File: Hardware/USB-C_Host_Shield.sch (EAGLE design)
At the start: 20 parts, among them U1 ARDUINO_UNO_R3_SHIELDBASIC, U4 AP7361C-33FGEUDFN-8

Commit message: Continued work on schematic
Working on importing new component now
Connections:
- net N$1 renamed VIN
- removed net N$9: C8.1, R1.2, U4.OUT
- new net GPX: U1.D8
- new net INT: U1.*D9
- new net MISO: U1.D12
- new net MOSI: U1.*D11
- new net N$15: U1.SDA
- new net N$16: U1.SCL
- new net RESET: U1.D7
- new net SCK: U1.D13
- new net SS: U1.*D10
- net 3.3V: now also C8.1, R1.2, U4.OUT
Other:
- moved on the sheet: U1
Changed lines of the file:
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@@
 <class number="0" name="default" width="0" drill="0">
+</class>
+<class number="1" name="VIN" width="0" drill="0">
 </class>
 </classes>
@@
 <part name="C6" library="SparkFun-Capacitors" deviceset="10UF-POLAR" device="-EIA3216-16V-10%(TANT)" value="10uF"/>
 <part name="GND3" library="SparkFun-PowerSymbols" deviceset="GND" device=""/>
-<part name="GND4" library="SparkFun-PowerSymbols" deviceset="GND" device=""/>
 <part name="C7" library="SparkFun-Capacitors" deviceset="10UF-POLAR" device="-EIA3216-16V-10%(TANT)" value="10uF"/>
 <part name="GND5" library="SparkFun-PowerSymbols" deviceset="GND" device=""/>
@@
 <part name="GND7" library="SparkFun-PowerSymbols" deviceset="GND" device=""/>
 <part name="R1" library="SparkFun-Resistors" deviceset="1KOHM" device="-0603-1/10W-1%" value="1k"/>
+<part name="GND4" library="SparkFun-PowerSymbols" deviceset="GND" device=""/>
+<part name="SUPPLY2" library="SparkFun-PowerSymbols" deviceset="3.3V" device=""/>
 </parts>
 <sheets>
@@
 <instance part="FD3" gate="G$1" x="226.06" y="30.48" smashed="yes"/>
 <instance part="FD4" gate="G$1" x="231.14" y="27.94" smashed="yes"/>
-<instance part="U1" gate="G$1" x="48.26" y="96.52" smashed="yes">
-<attribute name="NAME" x="38.608" y="117.094" size="1.778" layer="95" font="vector"/>
-<attribute name="VALUE" x="39.37" y="70.866" size="1.778" layer="96" font="vector" align="top-left"/>
+<instance part="U1" gate="G$1" x="58.42" y="71.12" smashed="yes">
+<attribute name="NAME" x="48.768" y="91.694" size="1.778" layer="95" font="vector"/>
+<attribute name="VALUE" x="49.53" y="45.466" size="1.778" layer="96" font="vector" align="top-left"/>
 </instance>
 <instance part="J1" gate="J1" x="127" y="111.76" smashed="yes">
@@
 <attribute name="VALUE" x="193.04" y="124.206" size="1.778" layer="96" font="vector" align="top-center"/>
 </instance>
-<instance part="GND2" gate="1" x="30.48" y="66.04" smashed="yes">
-<attribute name="VALUE" x="30.48" y="65.786" size="1.778" layer="96" font="vector" align="top-center"/>
+<instance part="GND2" gate="1" x="40.64" y="40.64" smashed="yes">
+<attribute name="VALUE" x="40.64" y="40.386" size="1.778" layer="96" font="vector" align="top-center"/>
 </instance>
 <instance part="C6" gate="G$1" x="71.12" y="154.94" smashed="yes">
@@
 <attribute name="VALUE" x="66.04" y="139.446" size="1.778" layer="96" font="vector" align="top-center"/>
 </instance>
-<instance part="GND4" gate="1" x="83.82" y="132.08" smashed="yes">
-<attribute name="VALUE" x="83.82" y="131.826" size="1.778" layer="96" font="vector" align="top-center"/>
-</instance>
 <instance part="C7" gate="G$1" x="111.76" y="154.94" smashed="yes">
 <attribute name="NAME" x="112.776" y="155.575" size="1.778" layer="95" font="vector"/>
@@
 <attribute name="NAME" x="161.036" y="152.4" size="1.778" layer="95" font="vector" rot="R90" align="bottom-center"/>
 <attribute name="VALUE" x="164.084" y="152.4" size="1.778" layer="96" font="vector" rot="R90" align="top-center"/>
+</instance>
+<instance part="GND4" gate="1" x="93.98" y="134.62" smashed="yes">
+<attribute name="VALUE" x="93.98" y="134.366" size="1.778" layer="96" font="vector" align="top-center"/>
+</instance>
+<instance part="SUPPLY2" gate="G$1" x="162.56" y="162.56" smashed="yes">
+<attribute name="VALUE" x="162.56" y="165.354" size="1.778" layer="96" font="vector" align="bottom-center"/>
 </instance>
 </instances>
@@
 </busses>
 <nets>
-<net name="N$1" class="0">
+<net name="VIN" class="0">
 <segment>
 <pinref part="S1" gate="G$1" pin="2"/>
@@
 <junction x="33.02" y="157.48"/>
 <wire x1="22.86" y1="157.48" x2="33.02" y2="157.48" width="0.1524" layer="91"/>
+<label x="22.86" y="157.48" size="1.27" layer="95"/>
 </segment>
 </net>
@@
 <junction x="193.04" y="142.24"/>
 </segment>
+<segment>
+<wire x1="142.24" y1="160.02" x2="147.32" y2="160.02" width="0.1524" layer="91"/>
+<pinref part="U4" gate="G$1" pin="OUT"/>
+<pinref part="C8" gate="G$1" pin="1"/>
+<wire x1="147.32" y1="157.48" x2="147.32" y2="160.02" width="0.1524" layer="91"/>
+<wire x1="147.32" y1="160.02" x2="162.56" y2="160.02" width="0.1524" layer="91"/>
+<junction x="147.32" y="160.02"/>
+<wire x1="162.56" y1="160.02" x2="162.56" y2="157.48" width="0.1524" layer="91"/>
+<pinref part="R1" gate="G$1" pin="2"/>
+<wire x1="162.56" y1="160.02" x2="162.56" y2="162.56" width="0.1524" layer="91"/>
+<junction x="162.56" y="160.02"/>
+<pinref part="SUPPLY2" gate="G$1" pin="3.3V"/>
+</segment>
 </net>
 <net name="GND" class="0">
@@
 <pinref part="U1" gate="G$1" pin="GND@2"/>
 <pinref part="GND2" gate="1" pin="GND"/>
-<wire x1="35.56" y1="78.74" x2="30.48" y2="78.74" width="0.1524" layer="91"/>
-<wire x1="30.48" y1="78.74" x2="30.48" y2="76.2" width="0.1524" layer="91"/>
+<wire x1="45.72" y1="53.34" x2="40.64" y2="53.34" width="0.1524" layer="91"/>
+<wire x1="40.64" y1="53.34" x2="40.64" y2="50.8" width="0.1524" layer="91"/>
 <pinref part="U1" gate="G$1" pin="GND@1"/>
-<wire x1="30.48" y1="76.2" x2="30.48" y2="73.66" width="0.1524" layer="91"/>
-<wire x1="30.48" y1="73.66" x2="30.48" y2="68.58" width="0.1524" layer="91"/>
-<wire x1="35.56" y1="76.2" x2="30.48" y2="76.2" width="0.1524" layer="91"/>
-<junction x="30.48" y="76.2"/>
+<wire x1="40.64" y1="50.8" x2="40.64" y2="48.26" width="0.1524" layer="91"/>
+<wire x1="40.64" y1="48.26" x2="40.64" y2="43.18" width="0.1524" layer="91"/>
+<wire x1="45.72" y1="50.8" x2="40.64" y2="50.8" width="0.1524" layer="91"/>
+<junction x="40.64" y="50.8"/>
 <pinref part="U1" gate="G$1" pin="GND@0"/>
-<wire x1="35.56" y1="73.66" x2="30.48" y2="73.66" width="0.1524" layer="91"/>
-<junction x="30.48" y="73.66"/>
+<wire x1="45.72" y1="48.26" x2="40.64" y2="48.26" width="0.1524" layer="91"/>
+<junction x="40.64" y="48.26"/>
 </segment>
 <segment>
@@
 </segment>
 </net>
-<net name="N$4" class="0">
-<segment>
-<pinref part="U2" gate="G$1" pin="ADJ"/>
-<wire x1="83.82" y1="152.4" x2="83.82" y2="147.32" width="0.1524" layer="91"/>
-<wire x1="83.82" y1="147.32" x2="93.98" y2="147.32" width="0.1524" layer="91"/>
-<wire x1="93.98" y1="147.32" x2="93.98" y2="149.86" width="0.1524" layer="91"/>
-<wire x1="83.82" y1="147.32" x2="83.82" y2="144.78" width="0.1524" layer="91"/>
-<junction x="83.82" y="147.32"/>
-</segment>
-</net>
-<net name="N$5" class="0">
-<segment>
-<wire x1="83.82" y1="137.16" x2="83.82" y2="134.62" width="0.1524" layer="91"/>
-<pinref part="GND4" gate="1" pin="GND"/>
-</segment>
-</net>
 <net name="N$6" class="0">
 <segment>
@@
 </segment>
 </net>
-<net name="N$9" class="0">
-<segment>
-<wire x1="142.24" y1="160.02" x2="147.32" y2="160.02" width="0.1524" layer="91"/>
-<pinref part="U4" gate="G$1" pin="OUT"/>
-<pinref part="C8" gate="G$1" pin="1"/>
-<wire x1="147.32" y1="157.48" x2="147.32" y2="160.02" width="0.1524" layer="91"/>
-<wire x1="147.32" y1="160.02" x2="162.56" y2="160.02" width="0.1524" layer="91"/>
-<junction x="147.32" y="160.02"/>
-<wire x1="162.56" y1="160.02" x2="162.56" y2="157.48" width="0.1524" layer="91"/>
-<pinref part="R1" gate="G$1" pin="2"/>
-</segment>
-</net>
 <net name="N$7" class="0">
 <segment>
@@
 </segment>
 </net>
+<net name="N$4" class="0">
+<segment>
+<pinref part="U2" gate="G$1" pin="ADJ"/>
+<wire x1="83.82" y1="152.4" x2="83.82" y2="149.86" width="0.1524" layer="91"/>
+<wire x1="83.82" y1="149.86" x2="93.98" y2="149.86" width="0.1524" layer="91"/>
+<wire x1="93.98" y1="149.86" x2="93.98" y2="147.32" width="0.1524" layer="91"/>
+<wire x1="93.98" y1="149.86" x2="93.98" y2="152.4" width="0.1524" layer="91"/>
+<junction x="93.98" y="149.86"/>
+</segment>
+</net>
+<net name="N$5" class="0">
+<segment>
+<wire x1="93.98" y1="139.7" x2="93.98" y2="137.16" width="0.1524" layer="91"/>
+<pinref part="GND4" gate="1" pin="GND"/>
+</segment>
+</net>
+<net name="RESET" class="0">
+<segment>
+<pinref part="U1" gate="G$1" pin="D7"/>
+<wire x1="71.12" y1="68.58" x2="86.36" y2="68.58" width="0.1524" layer="91"/>
+<label x="76.2" y="68.58" size="1.778" layer="95"/>
+</segment>
+</net>
+<net name="GPX" class="0">
+<segment>
+<pinref part="U1" gate="G$1" pin="D8"/>
+<wire x1="71.12" y1="66.04" x2="86.36" y2="66.04" width="0.1524" layer="91"/>
+<label x="76.2" y="66.04" size="1.778" layer="95"/>
+</segment>
+</net>
+<net name="INT" class="0">
+<segment>
+<pinref part="U1" gate="G$1" pin="*D9"/>
+<wire x1="86.36" y1="63.5" x2="71.12" y2="63.5" width="0.1524" layer="91"/>
+<label x="76.2" y="63.5" size="1.778" layer="95"/>
+</segment>
+</net>
+<net name="SS" class="0">
+<segment>
+<pinref part="U1" gate="G$1" pin="*D10"/>
+<wire x1="71.12" y1="60.96" x2="86.36" y2="60.96" width="0.1524" layer="91"/>
+<label x="76.2" y="60.96" size="1.778" layer="95"/>
+</segment>
+</net>
+<net name="MOSI" class="0">
+<segment>
+<pinref part="U1" gate="G$1" pin="*D11"/>
+<wire x1="71.12" y1="58.42" x2="86.36" y2="58.42" width="0.1524" layer="91"/>
+<label x="76.2" y="58.42" size="1.778" layer="95"/>
+</segment>
+</net>
+<net name="MISO" class="0">
+<segment>
+<pinref part="U1" gate="G$1" pin="D12"/>
+<wire x1="71.12" y1="55.88" x2="86.36" y2="55.88" width="0.1524" layer="91"/>
+<label x="76.2" y="55.88" size="1.778" layer="95"/>
+</segment>
+</net>
+<net name="SCK" class="0">
+<segment>
+<pinref part="U1" gate="G$1" pin="D13"/>
+<wire x1="71.12" y1="53.34" x2="86.36" y2="53.34" width="0.1524" layer="91"/>
+<label x="76.2" y="53.34" size="1.778" layer="95"/>
+</segment>
+</net>
+<net name="N$15" class="0">
+<segment>
+<pinref part="U1" gate="G$1" pin="SDA"/>
+<wire x1="71.12" y1="50.8" x2="86.36" y2="50.8" width="0.1524" layer="91"/>
+</segment>
+</net>
+<net name="N$16" class="0">
+<segment>
+<pinref part="U1" gate="G$1" pin="SCL"/>
+<wire x1="71.12" y1="48.26" x2="86.36" y2="48.26" width="0.1524" layer="91"/>
+</segment>
+</net>

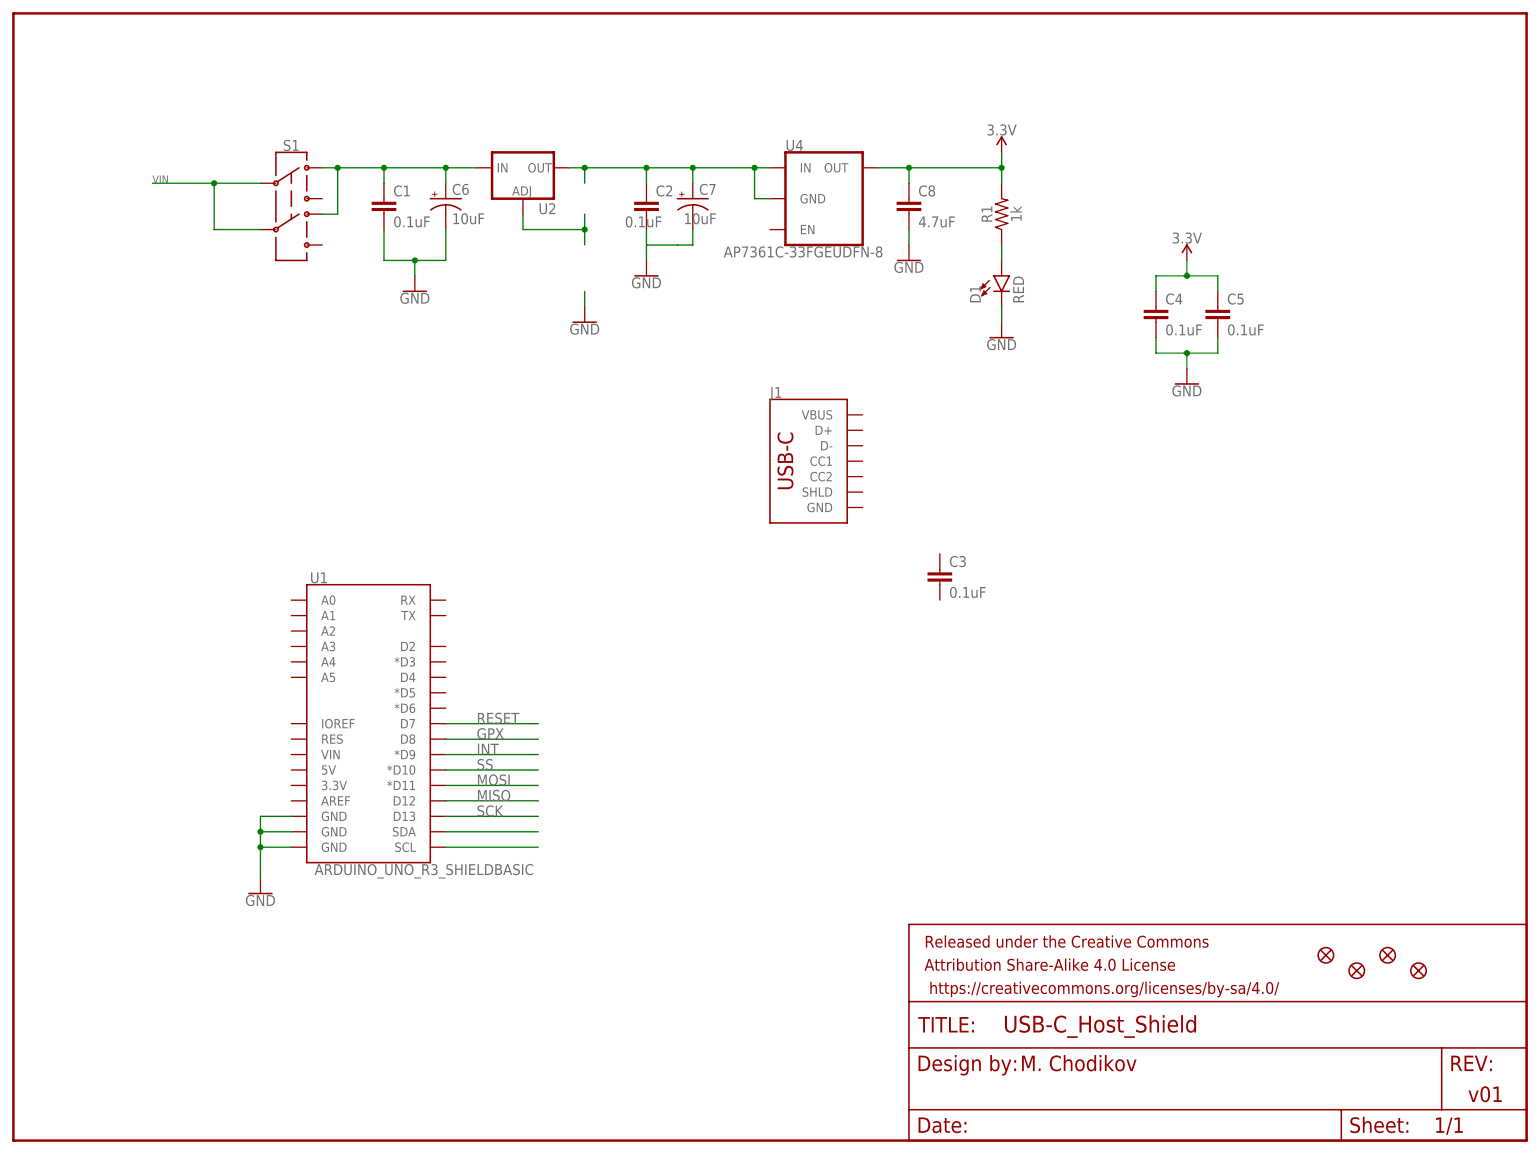
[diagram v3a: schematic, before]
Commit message: Worked on schematic
Updated SFE library with new branch for the MAX3421 component then added it to this project. Continued with other parts of schematic and cleaning up for easier reading/documentation
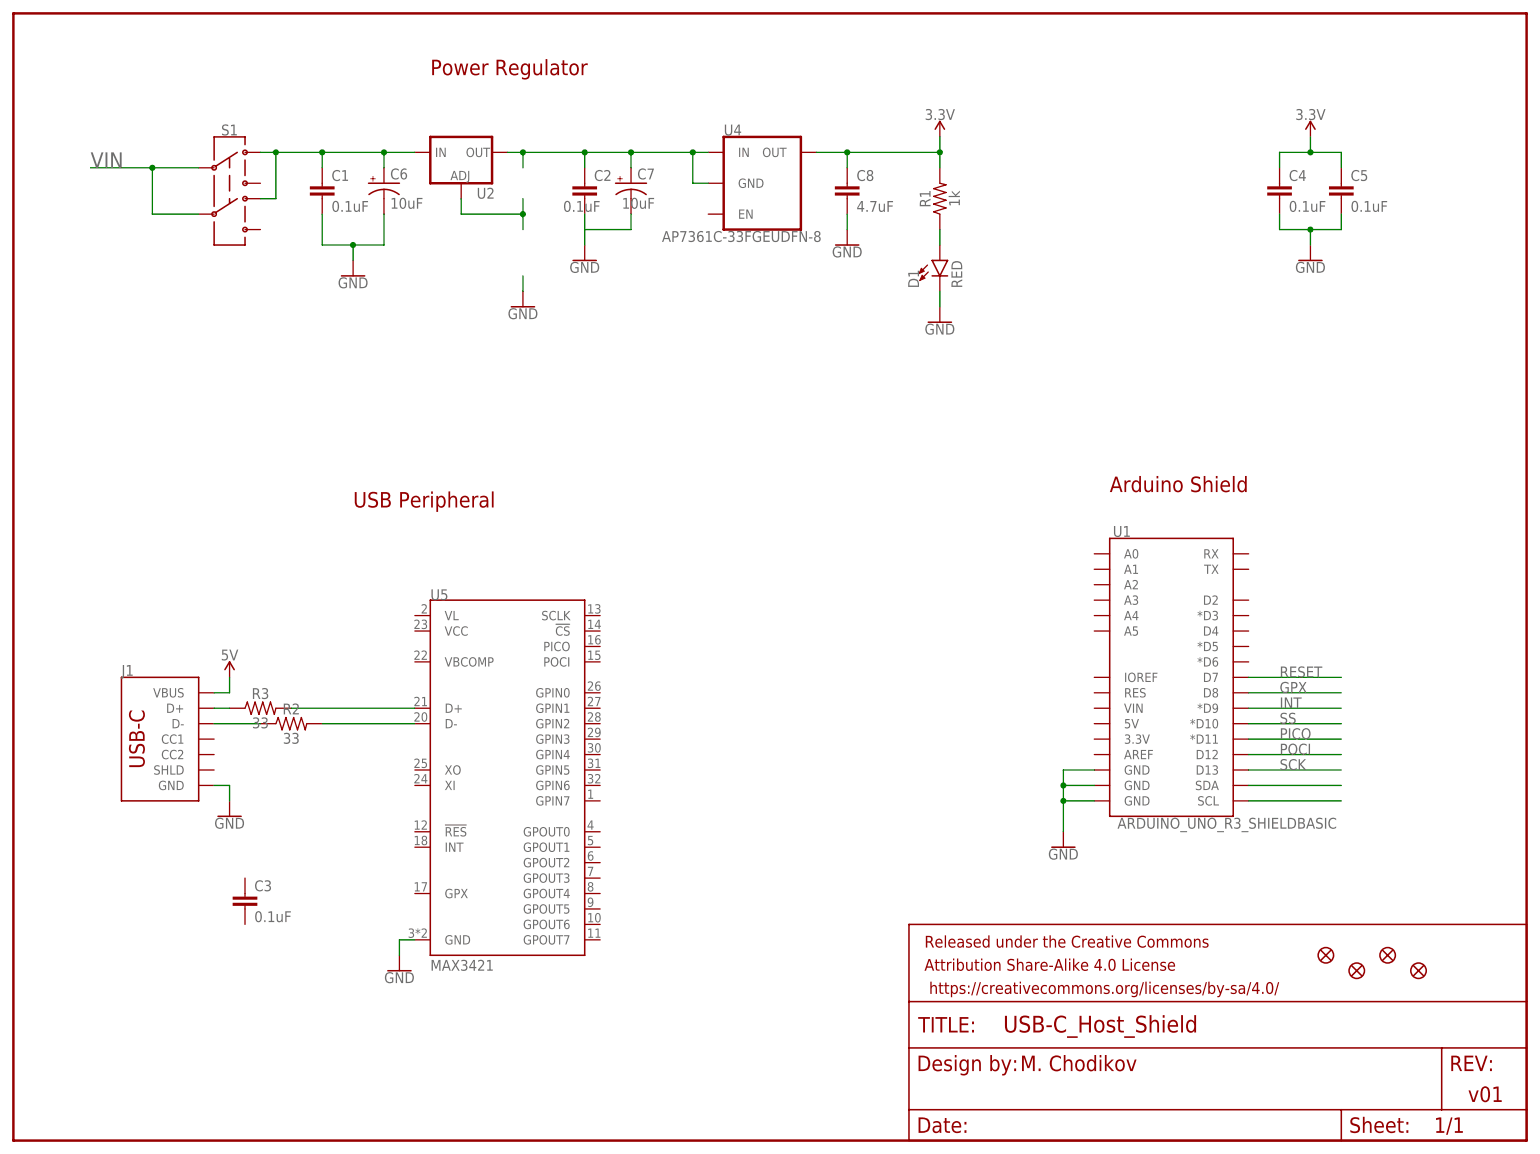
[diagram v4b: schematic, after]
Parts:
- added R2, R3: 33, SparkFun-Resistors:33OHM-0603-1/10W-1%
- added U5: MAX3421, SparkFun-IC-Microcontroller:MAX3421
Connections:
- net MISO renamed POCI
- net MOSI renamed PICO
- new net 5V: J1.VBUS
- new net N$1: J1.D+, R3.1
- new net N$10: R3.2, U5.D+
- new net N$11: J1.D-, R2.1
- new net N$9: R2.2, U5.D-
- net GND: now also J1.GND, U5.GND
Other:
- note added: "Arduino Shield"
- note added: "Power Regulator"
- note added: "USB Peripheral"
- moved on the sheet: C1, C2, C3, C4, C5, C6, C7, C8, D1, J1, R1, S1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
